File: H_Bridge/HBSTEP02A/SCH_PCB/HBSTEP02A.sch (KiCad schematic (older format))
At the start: 78 parts, among them J1 VIO 3.3-5V, J10 SDO/NAO/CFG0, J11 ENCN/DCO, J12 ENCB/DCEN/CFG4, J13 ENCA/DCIN/CFG5, J14 SWP/DIAG1, J15 SWN/DIAG0, J16 CONN1_1, J17 CONN1_1, J18 POWER SELECT, J19 SDMODE, J2 REFL/STEP, J20 DRV_ENN_CFG6, J21 SWSEL, J22 SPIMODE, J23 AIN, J24 CONN1_1, J25 CONN1_1, J3 REFR/DIR, J4 CLK, J5 CONN1_1, J6 CONN1_1, J7 CSN/CFG3, J8 SCK/CFG2, J9 SID/NAI/CFG1, M1 HOLE, M2 HOLE, M3 HOLE, M4 HOLE, U1 TMC5130A

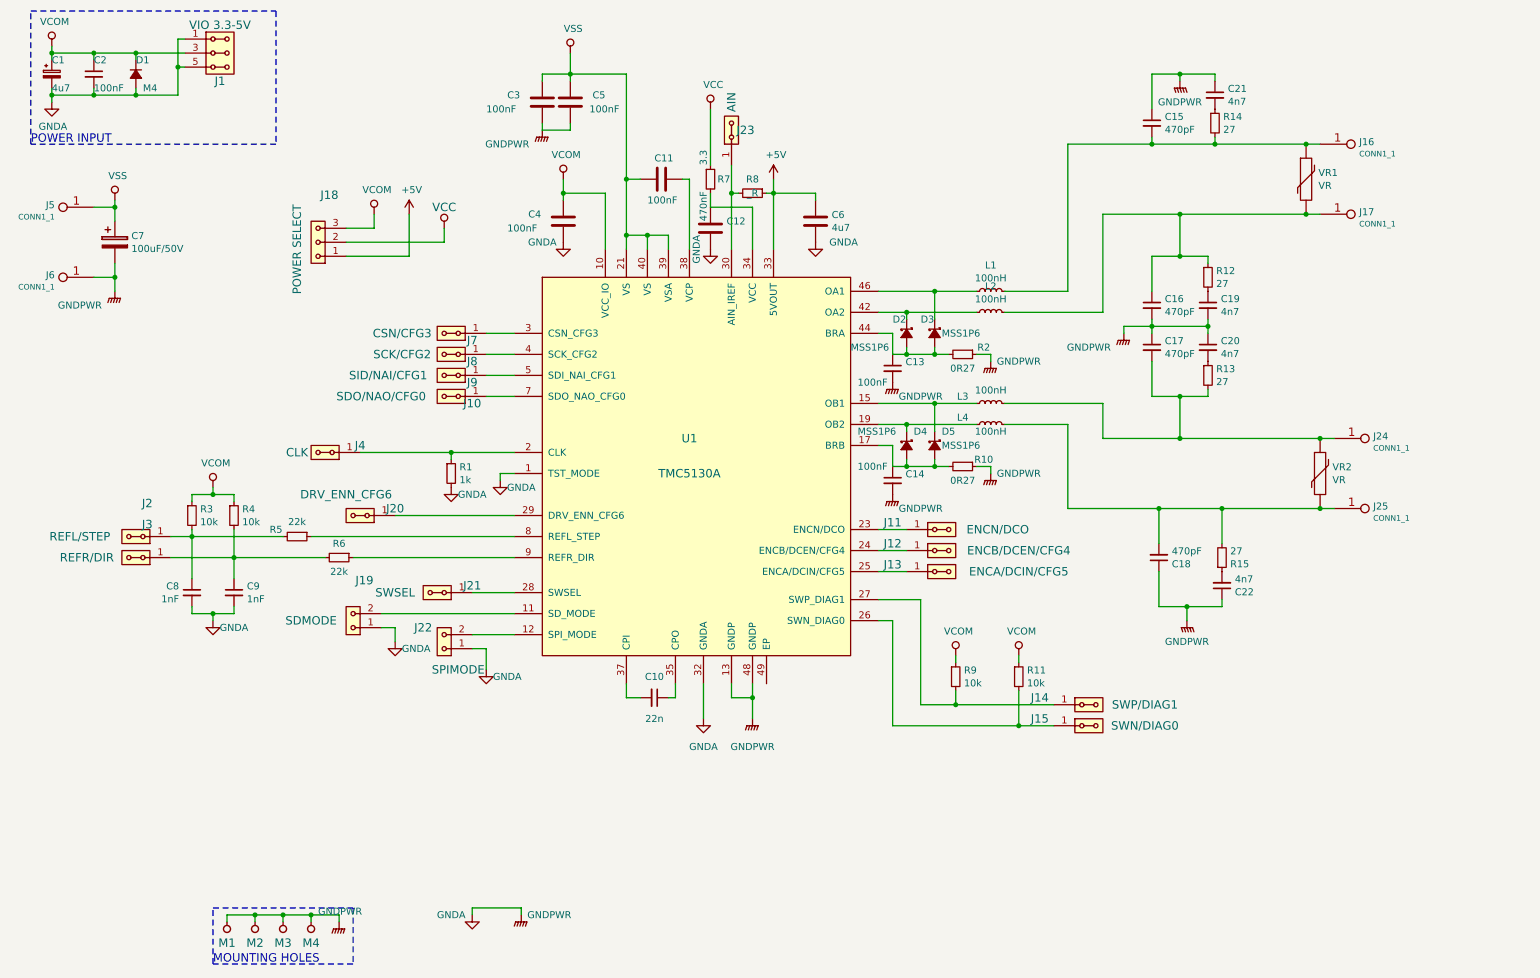
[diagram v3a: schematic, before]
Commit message: Vylepseni layoutu, popisku a vygenerovani vyrobnich podkladu.
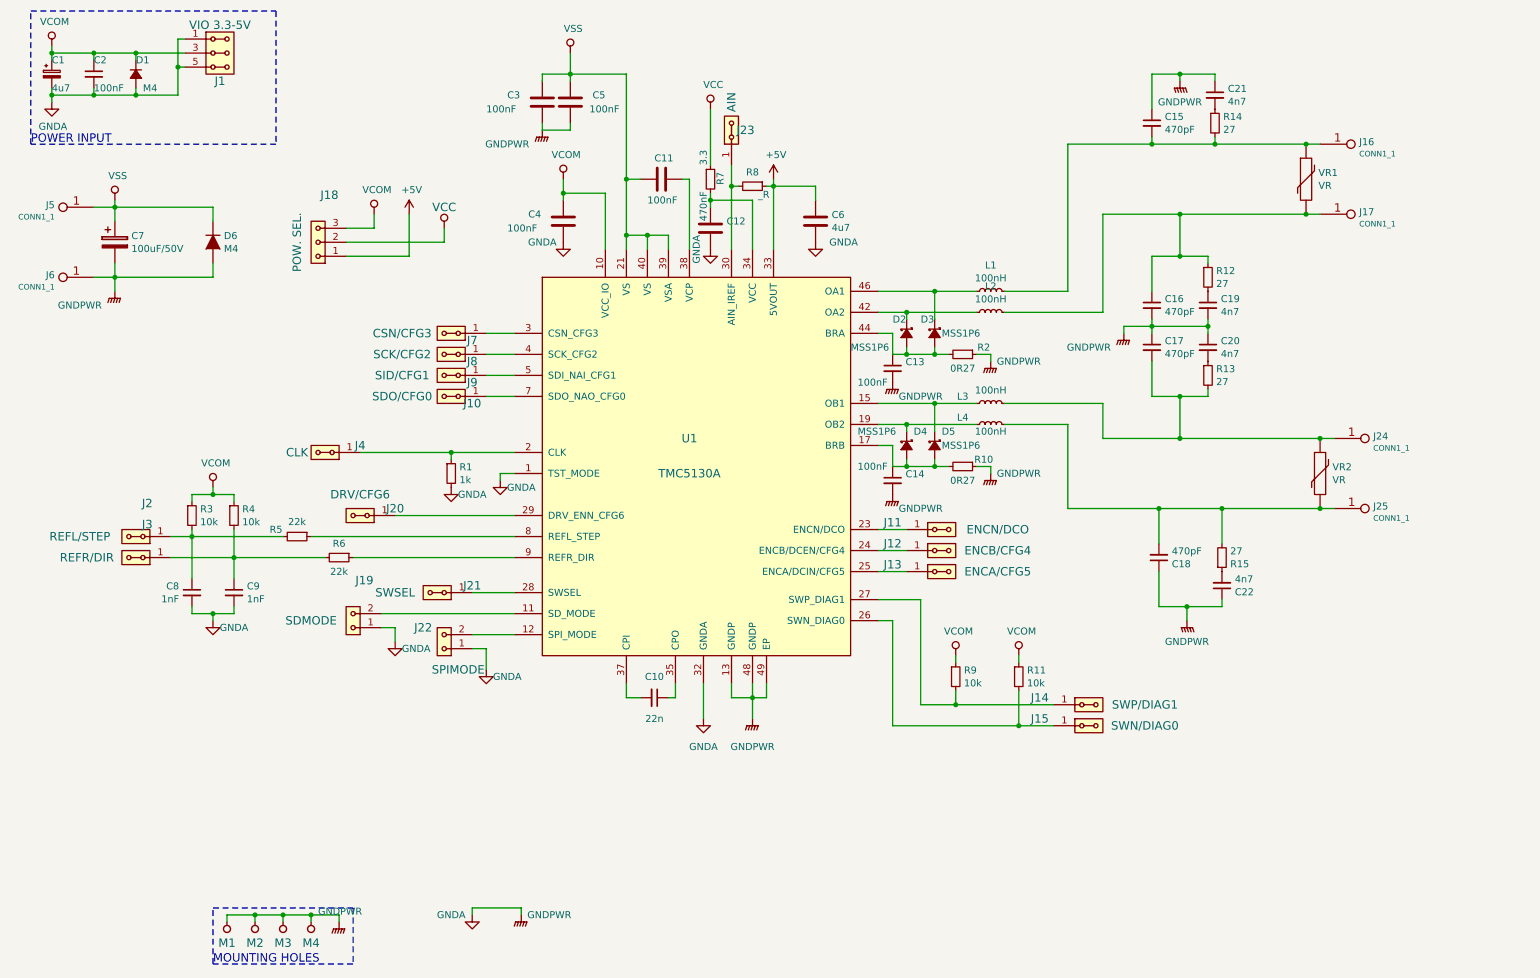
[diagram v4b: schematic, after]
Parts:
- added D6: M4, Diodes_SMD:SMB_Handsoldering, symbol D
- J10: value SDO/NAO/CFG0 -> SDO/CFG0
- J12: value ENCB/DCEN/CFG4 -> ENCB/CFG4
- J13: value ENCA/DCIN/CFG5 -> ENCA/CFG5
- J18: value POWER SELECT -> POW. SEL.
- J20: value DRV_ENN_CFG6 -> DRV/CFG6
- J9: value SID/NAI/CFG1 -> SID/CFG1
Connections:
- net GNDA: now also U1.49 (EP), D6.2 (A)
- net VSS: now also D6.1 (K)
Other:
- moved on the sheet: R8
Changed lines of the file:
@@
 LIBS:graphic
 LIBS:hc11
+LIBS:header
 LIBS:intel
 LIBS:interface
@@
 LIBS:logo
 LIBS:maxim
+LIBS:mechanical
 LIBS:memory
 LIBS:microchip_dspic33dsc
@@
 LIBS:xilinx
 LIBS:Zilog
+LIBS:MLAB_CONNECTORS
+LIBS:MLAB_Jumpers
 LIBS:HBSTEP02A-cache
 EELAYER 25 0
@@
 P 7250 4600
 F 0 "J12" H 6900 4650 60  0000 C CNN
-F 1 "ENCB/DCEN/CFG4" H 7800 4600 60  0000 C CNN
+F 1 "ENCB/CFG4" H 7650 4600 60  0000 C CNN
 F 2 "Mlab_Pin_Headers:Straight_1x02" H 7250 4600 60  0001 C CNN
 F 3 "" H 7250 4600 60  0000 C CNN
@@
 P 7250 4750
 F 0 "J13" H 6900 4800 60  0000 C CNN
-F 1 "ENCA/DCIN/CFG5" H 7800 4750 60  0000 C CNN
+F 1 "ENCA/CFG5" H 7650 4750 60  0000 C CNN
 F 2 "Mlab_Pin_Headers:Straight_1x02" H 7250 4750 60  0001 C CNN
 F 3 "" H 7250 4750 60  0000 C CNN
@@
 P 3750 3350
 F 0 "J9" H 3600 3400 60  0000 C CNN
-F 1 "SID/NAI/CFG1" H 4200 3350 60  0000 C CNN
+F 1 "SID/CFG1" H 4100 3350 60  0000 C CNN
 F 2 "Mlab_Pin_Headers:Straight_1x02" H 3750 3350 60  0001 C CNN
 F 3 "" H 3750 3350 60  0000 C CNN
@@
 P 3750 3500
 F 0 "J10" H 3600 3550 60  0000 C CNN
-F 1 "SDO/NAO/CFG0" H 4250 3500 60  0000 C CNN
+F 1 "SDO/CFG0" H 4100 3500 60  0000 C CNN
 F 2 "Mlab_Pin_Headers:Straight_1x02" H 3750 3500 60  0001 C CNN
 F 3 "" H 3750 3500 60  0000 C CNN
@@
 	4400 1600 4400 1550
 Wire Wire Line
-	6350 2050 6350 2100
-Wire Wire Line
-	6000 2050 6350 2050
+	6350 2000 6350 2100
 Wire Wire Line
 	6050 1950 6050 2450
@@
 	5900 5550 5900 5800
 Wire Wire Line
-	5750 5650 5900 5650
+	5750 5650 6000 5650
 Wire Wire Line
 	5750 5550 5750 5650
@@
 P 3100 4350
 F 0 "J20" H 2850 4300 60  0000 C CNN
-F 1 "DRV_ENN_CFG6" H 3200 4200 60  0000 C CNN
+F 1 "DRV/CFG6" H 3100 4200 60  0000 C CNN
 F 2 "Mlab_Pin_Headers:Straight_1x02" H 3100 4350 60  0001 C CNN
 F 3 "" H 3100 4350 60  0000 C CNN
@@
 $EndComp
 Wire Wire Line
-	1200 2150 1350 2150
+	1200 2150 2050 2150
 Wire Wire Line
 	1350 2100 1350 2250
@@
 	1350 2550 1350 2750
 Wire Wire Line
-	1350 2650 1200 2650
+	1200 2650 2050 2650
 $Comp
 L VSS #PWR027
@@
 L R_Small R8
 U 1 1 56E4E678
-P 5900 2050
-F 0 "R8" V 5800 2050 50  0000 C CNN
-F 1 "_R" V 5900 2050 50  0000 C CNN
-F 2 "Resistors_SMD:R_0805_HandSoldering" H 5900 2050 50  0001 C CNN
-F 3 "" H 5900 2050 50  0000 C CNN
-	1    5900 2050
+P 5900 2000
+F 0 "R8" V 5800 2000 50  0000 C CNN
+F 1 "_R" V 5960 2080 50  0000 C CNN
+F 2 "Resistors_SMD:R_0805_HandSoldering" H 5900 2000 50  0001 C CNN
+F 3 "" H 5900 2000 50  0000 C CNN
+	1    5900 2000
 	0    1    1    0
 $EndComp
-Connection ~ 6050 2050
-Wire Wire Line
-	5800 2050 5750 2050
+Connection ~ 6050 2000
 Wire Wire Line
 	5750 1850 5750 2450
@@
 	0    -1   -1   0
 $EndComp
-Connection ~ 5750 2050
+Connection ~ 5750 2000
 $Comp
 L VCC #PWR030
@@
 P 2800 2400
 F 0 "J18" H 2719 2063 60  0000 C CNN
-F 1 "POWER SELECT" V 2950 2450 60  0000 C CNN
+F 1 "POW. SEL." V 2950 2400 60  0000 C CNN
 F 2 "Mlab_Pin_Headers:Straight_1x03" H 2800 2500 60  0001 C CNN
 F 3 "" H 2800 2500 60  0000 C CNN
@@
 U 1 1 56E593E1
 P 5600 1950
-F 0 "R7" H 5650 1950 50  0000 L CNN
+F 0 "R7" V 5670 1910 50  0000 L CNN
 F 1 "3.3" V 5550 2050 50  0000 L CNN
 F 2 "Resistors_SMD:R_0805" H 5600 1950 50  0001 C CNN
@@
 	5600 1850 5600 1450
 Wire Wire Line
-	5600 2150 5900 2150
-Wire Wire Line
-	5900 2150 5900 2450
+	5900 2100 5900 2450
 Wire Wire Line
 	3000 2400 3700 2400
@@
 Wire Wire Line
 	3200 2300 3000 2300
+Wire Wire Line
+	5600 2100 5900 2100
+Connection ~ 5600 2100
+Wire Wire Line
+	6000 2000 6350 2000
+Wire Wire Line
+	5800 2000 5750 2000
+Wire Wire Line
+	6000 5650 6000 5550
+$Comp
+L D D6
+U 1 1 56E6F352
+P 2050 2400
+F 0 "D6" V 2004 2478 50  0000 L CNN
+F 1 "M4" V 2096 2478 50  0000 L CNN
+F 2 "Diodes_SMD:SMB_Handsoldering" H 2050 2400 50  0001 C CNN
+F 3 "" H 2050 2400 50  0000 C CNN
+	1    2050 2400
+	0    1    1    0
+$EndComp
+Wire Wire Line
+	2050 2650 2050 2550
+Wire Wire Line
+	2050 2150 2050 2250
 $EndSCHEMATC
